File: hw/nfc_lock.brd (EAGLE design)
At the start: 49.2 x 76.2 mm, 30 parts, among them IC1 STM8S003F3, IC3 MCP170312MB, Q1 8MHz, U1 M24SR16-YMN6T/2, U2 IRFML8244TRPBF, U3 IRFML8244TRPBF, U4 2N7002BKW, X1 MINI-USB-32005-301

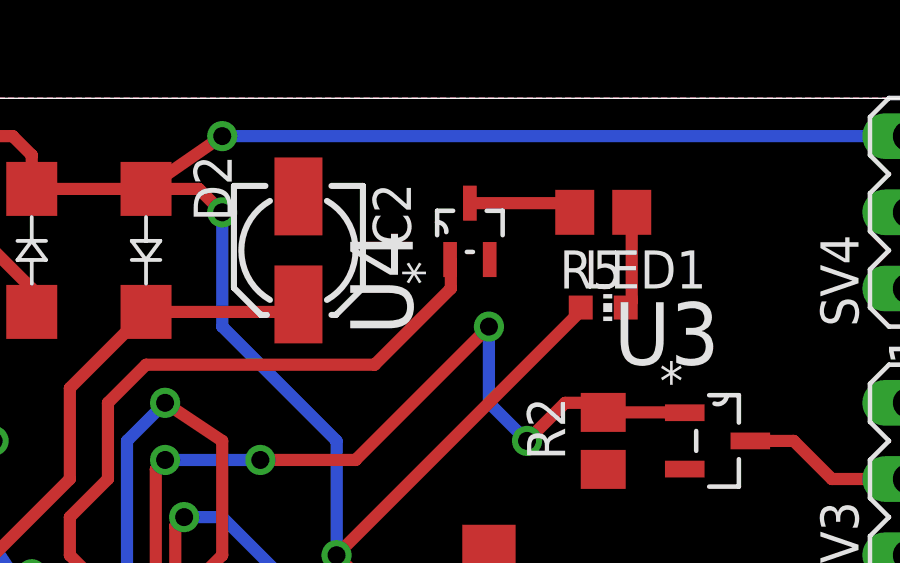
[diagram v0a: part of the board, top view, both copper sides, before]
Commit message: fixed packaging of 2n7002 transistor
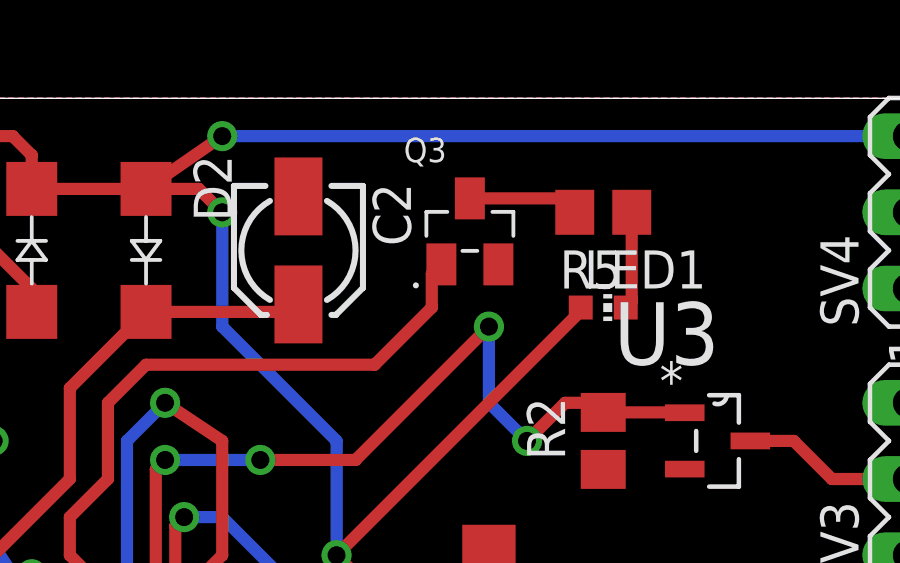
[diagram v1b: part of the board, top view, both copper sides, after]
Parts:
- removed U4: 2N7002BKW, 2n7002:SOT65P210X110-3N
- added Q3: 2N7002,215, Common-Parts-Library-Eagle:SOT95P230X110-3N
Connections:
- net 0V: now also Q3.2; no longer U4.2
- net N$14: now also Q3.3; no longer U4.3
- net N$19: now also Q3.1; no longer U4.1
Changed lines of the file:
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@@
 <layer number="45" name="Holes" color="7" fill="1" visible="no" active="yes"/>
 <layer number="46" name="Milling" color="3" fill="1" visible="no" active="yes"/>
-<layer number="47" name="Measures" color="7" fill="1" visible="yes" active="yes"/>
-<layer number="48" name="Document" color="7" fill="1" visible="yes" active="yes"/>
-<layer number="49" name="Reference" color="7" fill="1" visible="yes" active="yes"/>
+<layer number="47" name="Measures" color="7" fill="1" visible="no" active="yes"/>
+<layer number="48" name="Document" color="7" fill="1" visible="no" active="yes"/>
+<layer number="49" name="Reference" color="7" fill="1" visible="no" active="yes"/>
 <layer number="50" name="dxf" color="7" fill="1" visible="no" active="yes"/>
 <layer number="51" name="tDocu" color="7" fill="1" visible="yes" active="yes"/>
@@
 <layer number="123" name="tTestmark" color="7" fill="1" visible="no" active="yes"/>
 <layer number="124" name="bTestmark" color="7" fill="1" visible="no" active="yes"/>
-<layer number="125" name="_tNames" color="7" fill="1" visible="yes" active="yes"/>
-<layer number="126" name="_bNames" color="7" fill="1" visible="yes" active="yes"/>
-<layer number="127" name="_tValues" color="7" fill="1" visible="yes" active="yes"/>
-<layer number="128" name="_bValues" color="7" fill="1" visible="yes" active="yes"/>
+<layer number="125" name="_tNames" color="7" fill="1" visible="no" active="yes"/>
+<layer number="126" name="_bNames" color="7" fill="1" visible="no" active="yes"/>
+<layer number="127" name="_tValues" color="7" fill="1" visible="no" active="yes"/>
+<layer number="128" name="_bValues" color="7" fill="1" visible="no" active="yes"/>
 <layer number="129" name="Mask" color="7" fill="1" visible="no" active="yes"/>
 <layer number="131" name="tAdjust" color="7" fill="1" visible="no" active="yes"/>
@@
 </element>
 <element name="R4" library="rcl" package="R0805" value="20k" x="13.97" y="45.72" rot="R90"/>
-<element name="U4" library="2n7002" package="SOT65P210X110-3N" value="2N7002BKW" x="34.925" y="75.565" rot="R90">
-<attribute name="SUPPLIER" value="NXP Semiconductors" x="34.925" y="75.565" size="1.778" layer="27" rot="R90" display="off"/>
-<attribute name="OC_FARNELL" value="1894713" x="34.925" y="75.565" size="1.778" layer="27" rot="R90" display="off"/>
-<attribute name="PACKAGE" value="SOT-3" x="34.925" y="75.565" size="1.778" layer="27" rot="R90" display="off"/>
-<attribute name="OC_NEWARK" value="55T7739" x="34.925" y="75.565" size="1.778" layer="27" rot="R90" display="off"/>
-<attribute name="MPN" value="2N7002BKW" x="34.925" y="75.565" size="1.778" layer="27" rot="R90" display="off"/>
-</element>
 <element name="LED1" library="led" package="CHIP-LED0603" value="RED" x="39.37" y="73.025" rot="R270"/>
 <element name="R5" library="rcl" package="R0805" value="470R" x="39.37" y="76.2" rot="R180"/>
@@
 <attribute name="MF" value="" x="49.53" y="57.15" size="1.778" layer="27" rot="R90" display="off"/>
 <attribute name="MPN" value="" x="49.53" y="57.15" size="1.778" layer="27" rot="R90" display="off"/>
+</element>
+<element name="Q3" library="Common-Parts-Library-Eagle" package="SOT95P230X110-3N" value="2N7002,215" x="34.925" y="75.565">
+<attribute name="MANUFACTURER" value="NXP Semiconductor" x="34.925" y="75.565" size="1.778" layer="27" display="off"/>
 </element>
 </elements>
@@
 <contactref element="SV3" pad="1"/>
 <contactref element="SV1" pad="1"/>
-<contactref element="U4" pad="2"/>
 <contactref element="C4" pad="-"/>
 <contactref element="C5" pad="1"/>
@@
 <wire x1="19.05" y1="59.69" x2="17.91" y2="59.69" width="0.4064" layer="1"/>
 <wire x1="17.91" y1="59.69" x2="17.78" y2="59.82" width="0.4064" layer="1"/>
+<contactref element="Q3" pad="2"/>
 </signal>
 <signal name="+5V/1">
@@
 <signal name="N$14">
 <contactref element="R5" pad="2"/>
-<contactref element="U4" pad="3"/>
-<wire x1="34.925" y1="76.5048" x2="38.1152" y2="76.5048" width="0.4064" layer="1"/>
 <wire x1="38.1152" y1="76.5048" x2="38.42" y2="76.2" width="0.4064" layer="1"/>
+<contactref element="Q3" pad="3"/>
+<wire x1="34.925" y1="76.665" x2="37.955" y2="76.665" width="0.4064" layer="1"/>
+<wire x1="37.955" y1="76.665" x2="38.42" y2="76.2" width="0.4064" layer="1"/>
 </signal>
 <signal name="N$15">
@@
 <signal name="N$19">
 <contactref element="IC1" pad="16"/>
-<contactref element="U4" pad="1"/>
 <wire x1="24.13" y1="71.12" x2="31.75" y2="71.12" width="0.4064" layer="1"/>
-<wire x1="31.75" y1="71.12" x2="34.29" y2="73.66" width="0.4064" layer="1"/>
-<wire x1="34.29" y1="73.66" x2="34.29" y2="74.5998" width="0.4064" layer="1"/>
-<wire x1="34.29" y1="74.5998" x2="34.2646" y2="74.6252" width="0.4064" layer="1"/>
 <wire x1="23.805" y1="60.0678" x2="23.805" y2="62.555" width="0.4064" layer="1"/>
 <wire x1="23.805" y1="62.555" x2="21.59" y2="64.77" width="0.4064" layer="1"/>
@@
 <wire x1="22.86" y1="67.31" x2="22.86" y2="69.85" width="0.4064" layer="1"/>
 <wire x1="22.86" y1="69.85" x2="24.13" y2="71.12" width="0.4064" layer="1"/>
+<contactref element="Q3" pad="1"/>
+<wire x1="31.75" y1="71.12" x2="33.655" y2="73.025" width="0.4064" layer="1"/>
+<wire x1="33.655" y1="73.025" x2="33.655" y2="74.145" width="0.4064" layer="1"/>
+<wire x1="33.655" y1="74.145" x2="33.975" y2="74.465" width="0.4064" layer="1"/>
 </signal>
 </signals>

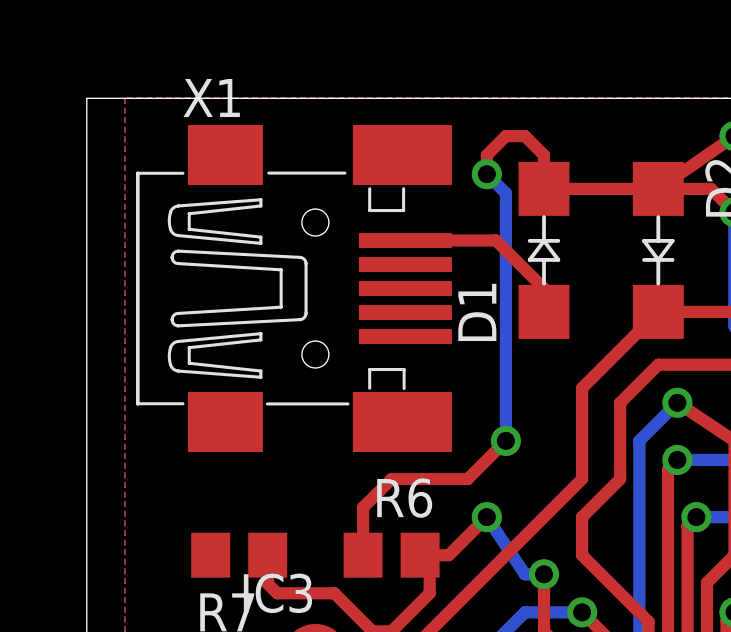
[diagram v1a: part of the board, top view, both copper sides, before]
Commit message: USB moved to the very edge of the board
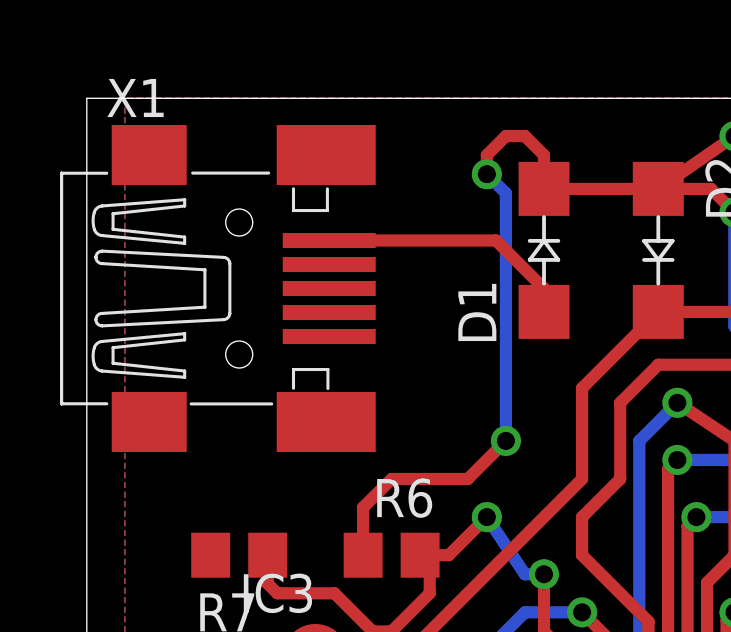
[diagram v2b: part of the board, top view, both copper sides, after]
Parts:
- moved X1 2.54 mm to (10.2, 73.7)
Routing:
- net +5V: track 6.06 -> 8.60 mm
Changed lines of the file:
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@@
 <element name="D1" library="diode" package="SMA-DO214AC" value="GF1" x="20.32" y="74.93" rot="R90"/>
 <element name="D2" library="diode" package="SMA-DO214AC" value="GF1" x="24.13" y="74.93" rot="R270"/>
-<element name="X1" library="con-cypressindustries" package="32005-301" value="MINI-USB-32005-301" x="12.7" y="73.66">
-<attribute name="OC_FARNELL" value="unknown" x="12.7" y="73.66" size="1.778" layer="27" display="off"/>
-<attribute name="MPN" value="" x="12.7" y="73.66" size="1.778" layer="27" display="off"/>
-<attribute name="MF" value="" x="12.7" y="73.66" size="1.778" layer="27" display="off"/>
-<attribute name="OC_NEWARK" value="unknown" x="12.7" y="73.66" size="1.778" layer="27" display="off"/>
+<element name="X1" library="con-cypressindustries" package="32005-301" value="MINI-USB-32005-301" x="10.16" y="73.66">
+<attribute name="OC_FARNELL" value="unknown" x="10.16" y="73.66" size="1.778" layer="27" display="off"/>
+<attribute name="MPN" value="" x="10.16" y="73.66" size="1.778" layer="27" display="off"/>
+<attribute name="MF" value="" x="10.16" y="73.66" size="1.778" layer="27" display="off"/>
+<attribute name="OC_NEWARK" value="unknown" x="10.16" y="73.66" size="1.778" layer="27" display="off"/>
 </element>
 <element name="R1" library="rcl" package="R0805" value="10k" x="17.145" y="52.07"/>
@@
 <contactref element="D1" pad="A"/>
 <contactref element="X1" pad="1"/>
-<wire x1="15.7" y1="75.26" x2="18.72" y2="75.26" width="0.4064" layer="1"/>
+<wire x1="13.16" y1="75.26" x2="18.72" y2="75.26" width="0.4064" layer="1"/>
 <wire x1="18.72" y1="75.26" x2="20.32" y2="73.66" width="0.4064" layer="1"/>
 <wire x1="20.32" y1="73.66" x2="20.32" y2="72.88" width="0.4064" layer="1"/>

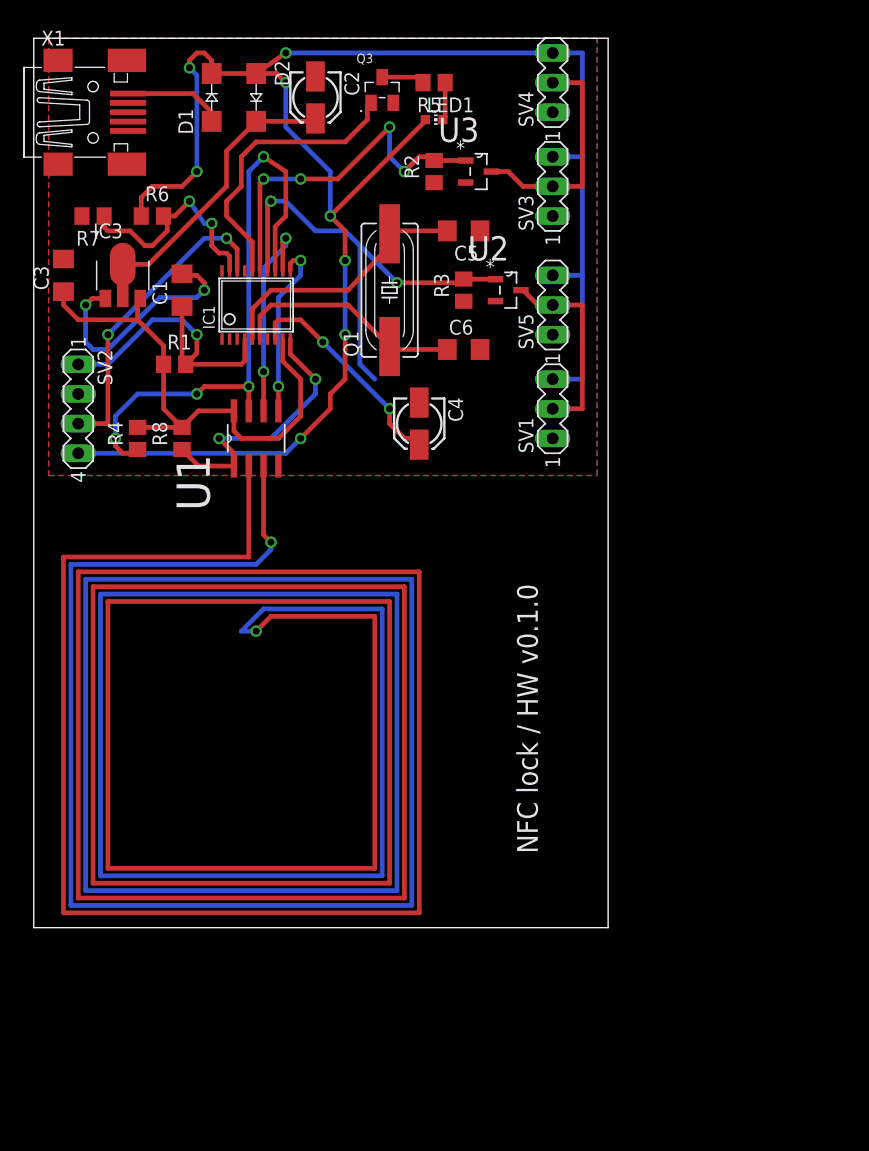
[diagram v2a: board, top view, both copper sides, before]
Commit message: bard dimentions decreased even further
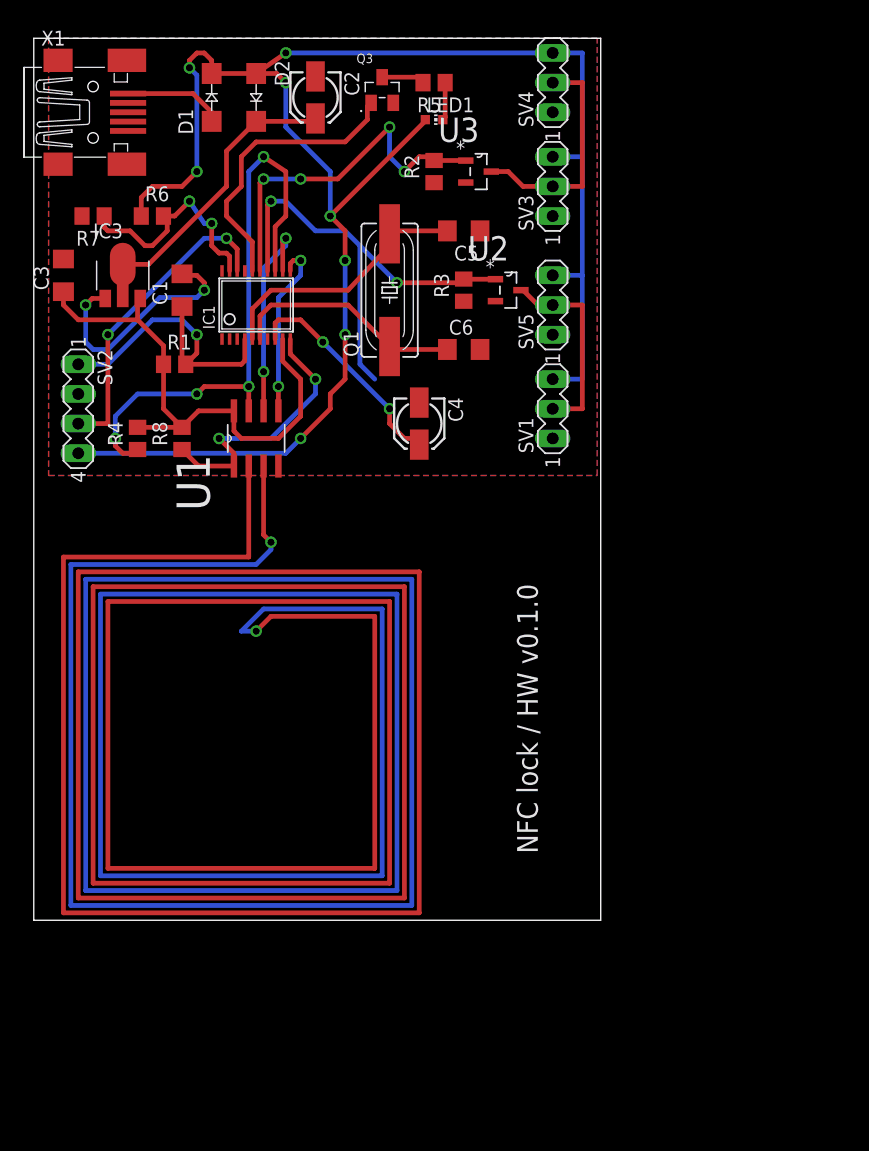
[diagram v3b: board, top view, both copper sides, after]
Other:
- board size 49.2 x 76.2 mm -> 48.6 x 75.6 mm
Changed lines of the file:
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@@
 <board>
 <plain>
-<wire x1="5.08" y1="3.81" x2="54.28" y2="3.81" width="0" layer="20"/>
-<wire x1="54.28" y1="3.81" x2="54.28" y2="80" width="0" layer="20"/>
-<wire x1="54.28" y1="80" x2="5.08" y2="80" width="0" layer="20"/>
-<wire x1="5.08" y1="80" x2="5.08" y2="3.81" width="0" layer="20"/>
+<wire x1="5.08" y1="4.445" x2="53.645" y2="4.445" width="0" layer="20"/>
+<wire x1="53.645" y1="4.445" x2="53.645" y2="80" width="0" layer="20"/>
+<wire x1="53.645" y1="80" x2="5.08" y2="80" width="0" layer="20"/>
+<wire x1="5.08" y1="80" x2="5.08" y2="4.445" width="0" layer="20"/>
 <text x="48.26" y="10.16" size="1.778" layer="25" rot="R90">NFC lock / HW v0.1.0</text>
 </plain>

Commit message: adjusted sizes of different components to match what i have in a closet... ;)
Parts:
- removed C6: 33pF, rcl:C1206
- added C8: 33pF, rcl:C0402
- C1: device rcl:C1206 -> rcl:C0603K
- C5: device rcl:C1206 -> rcl:C0402
- moved C5 10.2 mm to (40.6, 53.3)
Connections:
- net 0V: now also C8.1; no longer C6.2
- net N$16: now also C8.2; no longer C5.2
- net N$17: now also C5.2; no longer C6.1
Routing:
- net N$5: track 27.5 -> 28.3 mm
- net N$17: track 20.0 -> 19.5 mm
- net N$16: track 22.7 -> 22.2 mm
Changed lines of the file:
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@@
 </element>
 <element name="R1" library="rcl" package="R0805" value="10k" x="17.145" y="52.07"/>
-<element name="C1" library="rcl" package="C1206" value="10nF" x="17.78" y="58.42" rot="R90"/>
+<element name="C1" library="rcl" package="C0603K" value="10nF" x="17.78" y="58.42" rot="R90"/>
 <element name="U3" library="irfml8244trpbf" package="SOT95P240X112-3N" value="IRFML8244TRPBF" x="43.18" y="68.58">
 <attribute name="PACKAGE" value="SOT-23-3" x="43.18" y="68.58" size="1.778" layer="27" display="off"/>
@@
 <attribute name="MPN" value="" x="35.56" y="58.42" size="1.778" layer="27" rot="R90" display="off"/>
 </element>
-<element name="C5" library="rcl" package="C1206" value="33pF" x="41.91" y="63.5" rot="R180"/>
-<element name="C6" library="rcl" package="C1206" value="33pF" x="41.91" y="53.34"/>
 <element name="R6" library="rcl" package="R0805" value="24k" x="15.24" y="64.77"/>
 <element name="R7" library="rcl" package="R0805" value="10k" x="10.16" y="64.77" rot="R180"/>
@@
 <attribute name="MANUFACTURER" value="NXP Semiconductor" x="34.925" y="75.565" size="1.778" layer="27" display="off"/>
 </element>
+<element name="C8" library="rcl" package="C0402" value="33pF" x="40.64" y="63.5" rot="R180"/>
+<element name="C5" library="rcl" package="C0402" value="33pF" x="40.64" y="53.34" rot="R180"/>
 </elements>
 <signals>
@@
 <contactref element="SV1" pad="1"/>
 <contactref element="C4" pad="-"/>
-<contactref element="C5" pad="1"/>
-<contactref element="C6" pad="2"/>
 <contactref element="R7" pad="2"/>
 <contactref element="SV4" pad="1"/>
@@
 <wire x1="19.685" y1="59.055" x2="19.05" y2="59.69" width="0.4064" layer="1"/>
 <wire x1="19.05" y1="59.69" x2="17.91" y2="59.69" width="0.4064" layer="1"/>
-<wire x1="17.91" y1="59.69" x2="17.78" y2="59.82" width="0.4064" layer="1"/>
+<wire x1="17.91" y1="59.69" x2="17.78" y2="59.295" width="0.4064" layer="1"/>
 <contactref element="Q3" pad="2"/>
+<contactref element="C8" pad="1"/>
+<contactref element="C5" pad="1"/>
 </signal>
 <signal name="+5V/1">
@@
 <contactref element="IC1" pad="4"/>
 <contactref element="SV2" pad="1"/>
-<wire x1="17.65" y1="57.15" x2="17.78" y2="57.02" width="0.4064" layer="1"/>
-<wire x1="17.78" y1="57.02" x2="17.78" y2="52.385" width="0.4064" layer="1"/>
+<wire x1="17.65" y1="57.15" x2="17.78" y2="57.545" width="0.4064" layer="1"/>
+<wire x1="17.78" y1="57.545" x2="17.78" y2="52.385" width="0.4064" layer="1"/>
 <wire x1="17.78" y1="52.385" x2="18.095" y2="52.07" width="0.4064" layer="1"/>
 <wire x1="23.155" y1="54.2322" x2="23.155" y2="52.365" width="0.4064" layer="1"/>
@@
 <contactref element="IC1" pad="5"/>
 <contactref element="Q1" pad="2"/>
-<contactref element="C5" pad="2"/>
-<wire x1="40.51" y1="63.5" x2="35.814" y2="63.5" width="0.4064" layer="1"/>
-<wire x1="35.814" y1="63.5" x2="35.56" y2="63.246" width="0.4064" layer="1"/>
 <wire x1="23.805" y1="54.2322" x2="23.805" y2="56.825" width="0.4064" layer="1"/>
 <wire x1="23.805" y1="56.825" x2="25.4" y2="58.42" width="0.4064" layer="1"/>
@@
 <wire x1="32.004" y1="58.42" x2="35.56" y2="62.23" width="0.4064" layer="1"/>
 <wire x1="35.56" y1="62.23" x2="35.56" y2="63.246" width="0.4064" layer="1"/>
+<contactref element="C8" pad="2"/>
+<wire x1="39.99" y1="63.5" x2="35.814" y2="63.5" width="0.4064" layer="1"/>
+<wire x1="35.814" y1="63.5" x2="35.56" y2="63.246" width="0.4064" layer="1"/>
 </signal>
 <signal name="N$17">
 <contactref element="IC1" pad="6"/>
 <contactref element="Q1" pad="1"/>
-<contactref element="C6" pad="1"/>
 <wire x1="24.455" y1="54.2322" x2="24.455" y2="56.205" width="0.4064" layer="1"/>
 <wire x1="24.455" y1="56.205" x2="25.4" y2="57.15" width="0.4064" layer="1"/>
 <wire x1="25.4" y1="57.15" x2="32.004" y2="57.15" width="0.4064" layer="1"/>
 <wire x1="32.004" y1="57.15" x2="35.56" y2="53.594" width="0.4064" layer="1"/>
-<wire x1="40.51" y1="53.34" x2="35.814" y2="53.34" width="0.4064" layer="1"/>
+<contactref element="C5" pad="2"/>
+<wire x1="39.99" y1="53.34" x2="35.814" y2="53.34" width="0.4064" layer="1"/>
 <wire x1="35.814" y1="53.34" x2="35.56" y2="53.594" width="0.4064" layer="1"/>
 </signal>
